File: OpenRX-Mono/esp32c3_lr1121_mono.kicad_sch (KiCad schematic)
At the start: 48 parts, among them T1 0900PC16J0042001E, U1 ESP32-C3FH4, U2 TLV75533PDQNR, U3 TS2306A 240GF MSM 9_C2976675, U4 LR1121IMLTRT, U5 OW7EL89CENUYO3YLC-32M, U7 RFX2401C, U8 SKY13414-485LF, X1 CJ17-400001010B20

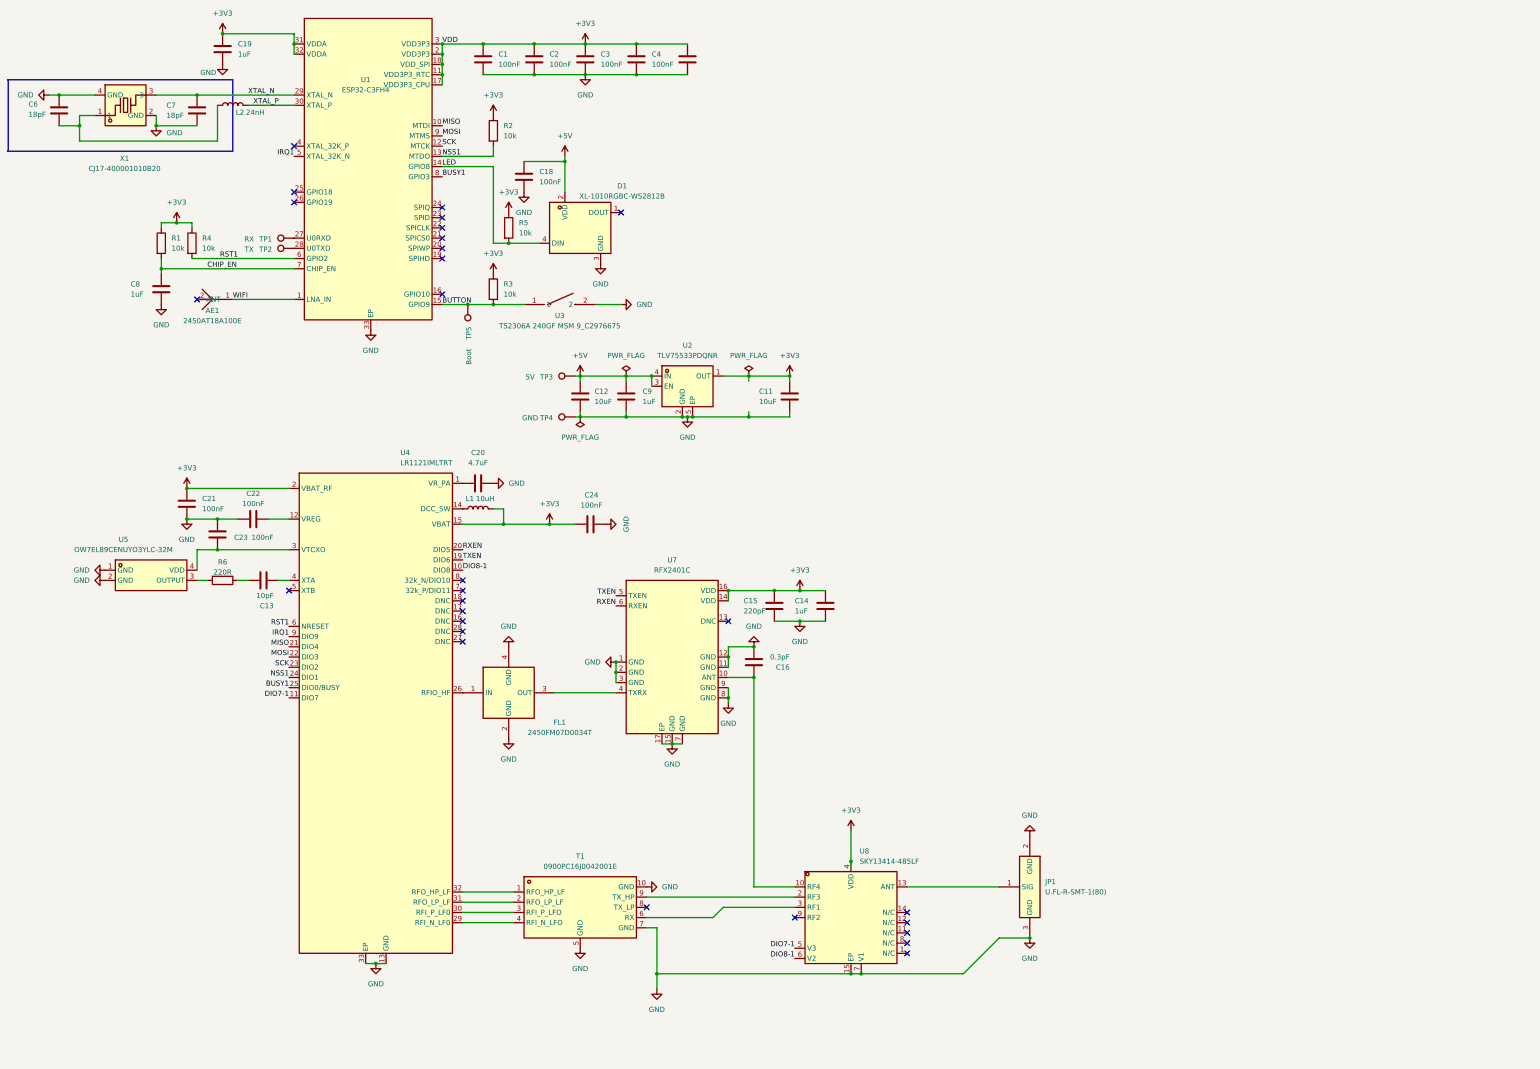
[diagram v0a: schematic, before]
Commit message: OpenRX Lite (UFL + molex)
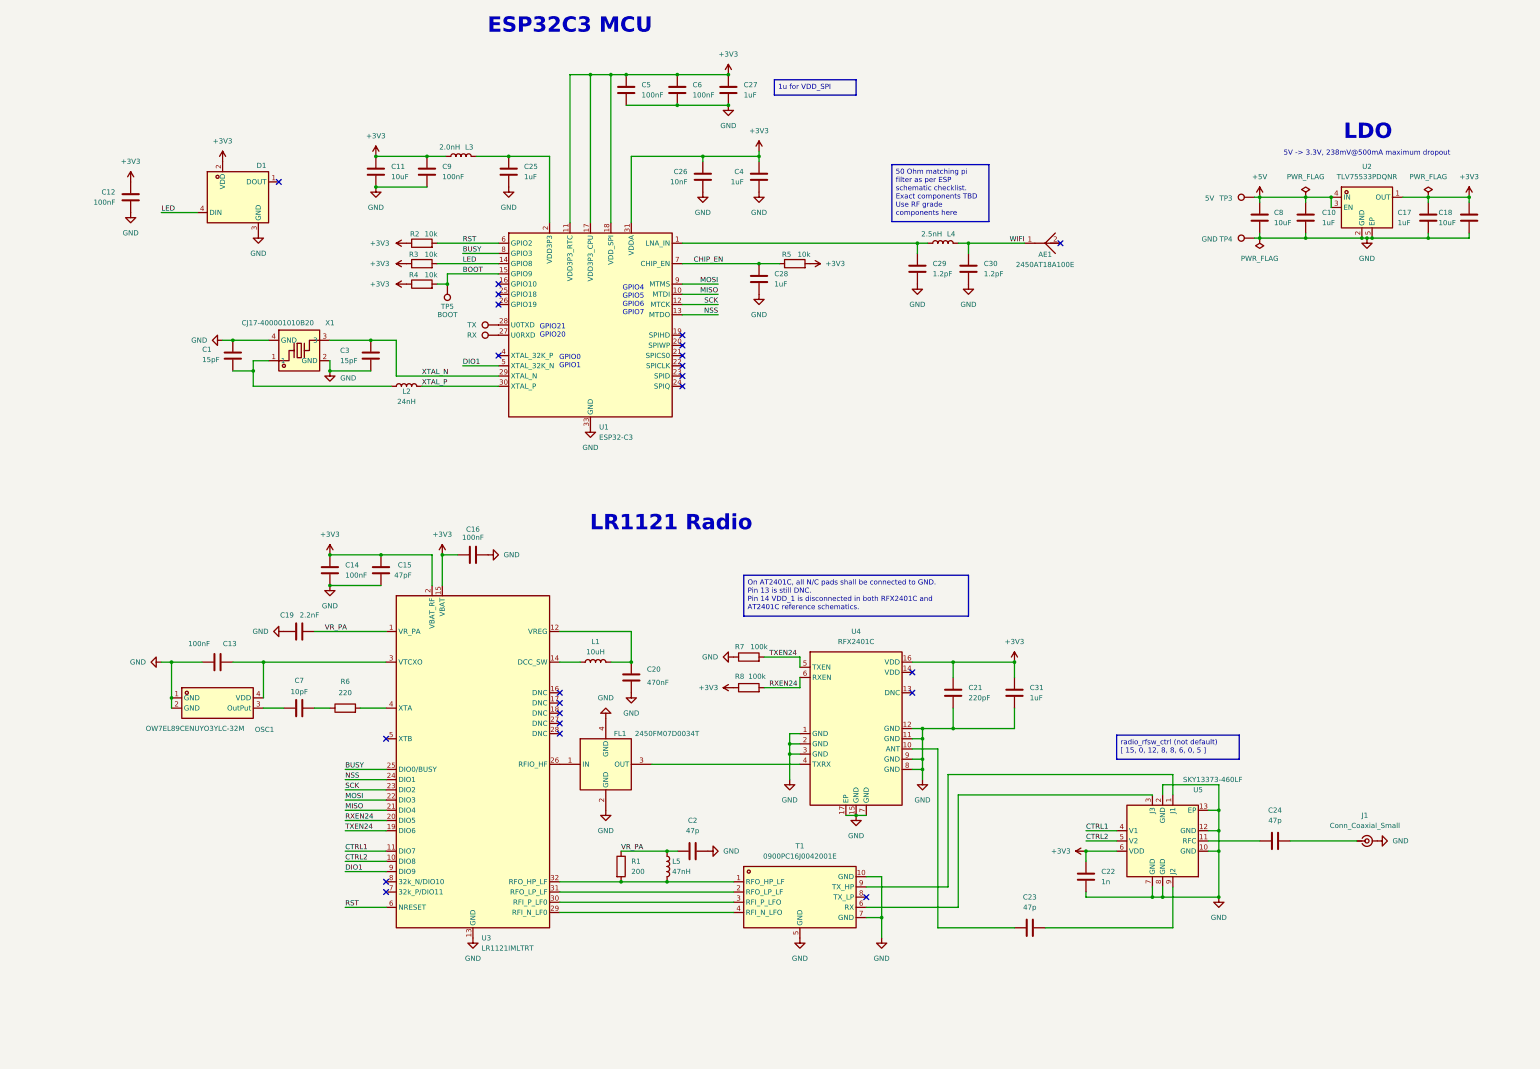
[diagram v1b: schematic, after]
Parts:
- removed JP1: U.FL-R-SMT-1(80), OpenRX-Shared:RF-SMD_FRF05002-JSS103M, symbol OpenRX-Shared:U.FL-R-SMT-1(80)
- removed U1: ESP32-C3FH4, OpenRX-Shared:QFN-32_L5.0-W5.0-P0.50-TL-EP3.7, symbol OpenRX-Shared:ESP32-C3FH4
- removed U3: TS2306A 240GF MSM 9_C2976675, OpenRX-Shared:SW-SMD_4P-L3.0-W2.0-P0.85-LS3.5, symbol OpenRX-Shared:TS2306A240GFMSM9_C2976675
- removed U4: LR1121IMLTRT, OpenRX-Shared:QFN-32_L5.0-W5.0-P0.50-BL-EP3.7, symbol OpenRX-Shared:LR1121IMLTRT
- removed U5: OW7EL89CENUYO3YLC-32M, OpenRX-Shared:OSC-SMD_4P-L2.0-W1.6-BL_TXC_7Z, symbol OpenRX-Shared:OW7EL89CENUYO3YLC-32M
- removed U7: RFX2401C, OpenRX-Shared:QFN-16_L3.0-W3.0-P0.50-BL-EP1.7, symbol OpenRX-Shared:RFX2401C
- removed U8: SKY13414-485LF, OpenRX-Shared:QFN-14_L2.0-W2.0-P0.45-BL-EP, symbol OpenRX-Shared:SKY13414-485LF
- added C10, C17, C25, C27, C28, C31: 1uF, Capacitor_SMD:C_0201_0603Metric, symbol Device:C
- added C26: 10nF, Capacitor_SMD:C_0201_0603Metric, symbol Device:C
- added C29, C30: 1.2pF, Capacitor_SMD:C_0201_0603Metric, symbol Device:C
- added J1: Conn_Coaxial_Small, Connector_Coaxial:U.FL_Hirose_U.FL-R-SMT-1_Vertical, symbol Connector:Conn_Coaxial_Small
- added L3: 2.0nH, Inductor_SMD:L_0201_0603Metric, symbol Device:L
- added L4: 2.5nH, Inductor_SMD:L_0201_0603Metric, symbol Device:L
- added L5: 47nH, Inductor_SMD:L_0402_1005Metric, symbol Device:L
- added OSC1: OW7EL89CENUYO3YLC-32M, OpenRX-Shared:OSC-SMD_4P-L2.0-W1.6-BL_TXC_7Z, symbol OpenRX-Shared:OW7EL89CENUYO3YLC-32M
- added R7, R8: 100k, Resistor_SMD:R_0201_0603Metric, symbol Device:R
- added U1: ESP32-C3, Package_DFN_QFN:QFN-32-1EP_5x5mm_P0.5mm_EP3.7x3.7mm, symbol MCU_Espressif:ESP32-C3
- added U3: LR1121IMLTRT, Package_DFN_QFN:QFN-32-1EP_5x5mm_P0.5mm_EP3.7x3.7mm, symbol OpenRX-Shared:LR1121IMLTRT
- added U4: RFX2401C, OpenRX-Shared:QFN-16_L3.0-W3.0-P0.50-BL-EP1.7, symbol OpenRX-Shared:RFX2401C
- added U5: SKY13373-460LF, OpenRX-Shared:QFN-12_EP_2x2_Pitch0.5mm, symbol OpenRX-Shared:SKY13373-460LF
- C1, C3: value 100nF -> 15pF; LCSC C76939 -> C85891; LCSC Part C76939 -> C85891
- C11: LCSC C15525 -> C76991; LCSC Part C15525 -> (none)
- C12: value 10uF -> 100nF; footprint Capacitor_SMD:C_0402_1005Metric -> Capacitor_SMD:C_0201_0603Metric; LCSC C15525 -> C76939; LCSC Part C15525 -> C76939
- C13: value 10pF -> 100nF; LCSC C76921 -> C76939; LCSC Part C76921 -> C76939
- C14, C9: value 1uF -> 100nF; LCSC C76935 -> C76939; LCSC Part C76935 -> C76939
- C15: value 220pF -> 47pF; LCSC C62548 -> C85908; LCSC Part C62548 -> C85908
- C16: value 0.3pF -> 100nF; LCSC C76927 -> C76939; LCSC Part C76927 -> C76939
- C18: value 100nF -> 10uF; footprint Capacitor_SMD:C_0201_0603Metric -> Capacitor_SMD:C_0402_1005Metric; LCSC C76939 -> C15525; LCSC Part C76939 -> C15525
- C19: value 1uF -> 2.2nF; LCSC C76935 -> C161488; LCSC Part C76935 -> (none)
- C2, C23, C24: value 100nF -> 47p; LCSC C76939 -> C85908; LCSC Part C76939 -> (none)
- C20: value 4.7uF -> 470nF; footprint Capacitor_SMD:C_0402_1005Metric -> Capacitor_SMD:C_0201_0603Metric; LCSC C23733 -> C85926; LCSC Part C23733 -> C85926
- C21: value 100nF -> 220pF; LCSC C76939 -> C907939; LCSC Part C76939 -> (none)
- C22: value 100nF -> 1n; LCSC C76939 -> C85934; LCSC Part C76939 -> (none)
- C4: value 100nF -> 1uF; LCSC C76939 -> C76935; LCSC Part C76939 -> C76935
- C6: value 18pF -> 100nF; LCSC C62164 -> C76939; LCSC Part C62164 -> C76939
- C7: value 18pF -> 10pF; LCSC C62164 -> C384956; LCSC Part C62164 -> C384956
- C8: value 1uF -> 10uF; footprint Capacitor_SMD:C_0201_0603Metric -> Capacitor_SMD:C_0402_1005Metric; LCSC C76935 -> C15525; LCSC Part C76935 -> C15525
- D1: LCSC C5349953 -> (none)
- L1: LCSC C1035 -> C194437; LCSC Part C1035 -> (none)
- R1: value 10k -> 200; LCSC C106225 -> C274337; LCSC Part C106225 -> (none)
- R6: value 220R -> 220; LCSC C274342 -> C2074788; LCSC Part C274342 -> C2074788
- T1: LCSC C19842466 -> (none)
- TP5: value Boot -> BOOT
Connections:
- net RST1 is gone; now on net BOOT: R4.2
- net +3V3: now also C12.1, C16.1, C18.1, C22.1, C6.1, C9.1, D1.2 (VDD), R5.2, C17.1, C26.1, C27.1, C31.1, L3.2, R8.1, U1.11 (VDD3P3_RTC), U1.17 (VDD3P3_CPU), U1.18 (VDD_SPI), U1.31 (VDDA), U1.32 (VDDA), U3.15 (VBAT), U3.2 (VBAT_RF), U4.16 (VDD), U5.6 (VDD); no longer C1.1, C19.1, C2.1, C24.2, C3.1, L1.2, R1.1, R5.1
- net +5V: now also C8.1, C10.1; no longer C12.1, C18.1, C9.1, D1.2 (VDD)
- net CHIP_EN: now also R5.1, C28.1, U1.7 (CHIP_EN); no longer C8.1, R1.2
- net LED: now also R3.2, U1.14 (GPIO8); no longer R5.2
- net MISO: now also U1.10 (MTDI), U3.21 (DIO4)
- net MOSI: now also U1.9 (MTMS), U3.22 (DIO3)
- net SCK: now also U1.12 (MTCK), U3.23 (DIO2)
- net WIFI: now also C30.1, L4.1
- net XTAL_N: now also C3.1, U1.29 (XTAL_N); no longer C7.1
- net XTAL_P: now also U1.30 (XTAL_P)
- net at TP1.1: now also U1.27 (U0RXD)
- net at TP2.1: now also U1.28 (U0TXD)
- net at L2.1, X1.1: now also C1.1; no longer C6.1
- net EP: now reaches C22.2
- net EP: now also C1.2, C11.2, C12.2, C13.1, C14.2, C15.2, C16.2, C18.2, C19.2, C2.2, C20.1, C21.2, C3.2, C4.2, C5.2, C6.2, C8.2, C9.2, D1.3 (GND), FL1.2 (GND), FL1.4 (GND), T1.10 (GND), T1.5 (GND), T1.7 (GND), TP4.1, U2.2 (GND), U2.5 (EP), X1.2 (GND), X1.4 (GND), C10.2, C17.2, C25.2, C26.2, C27.2, C28.2, C29.2, C30.2, C31.2, J1.2 (Ext), OSC1.1 (GND), OSC1.2 (GND), R7.1, U1.33 (GND), U3.13 (GND), U3.33 (EP), U4.1 (GND), U4.11 (GND), U4.12 (GND), U4.15 (GND), U4.17 (EP), U4.2 (GND), U4.3 (GND), U4.7 (GND), U4.8 (GND), U4.9 (GND), U5.10 (GND), U5.12 (GND), U5.13 (EP), U5.2 (GND), U5.7 (GND), U5.8 (GND)
- net at C23.2: now also U5.9 (J2)
- net at L1.1: now also U3.14 (DCC_SW)
- net at FL1.1 (IN): now also U3.26 (RFIO_HF)
- net at T1.4 (RFI_N_LFO): now also U3.29 (RFI_N_LF0)
- net at T1.3 (RFI_P_LFO): now also U3.30 (RFI_P_LF0)
- net at T1.2 (RFO_LP_LF): now also U3.31 (RFO_LP_LF)
- net at T1.1 (RFO_HP_LF): now also R1.2, L5.2, U3.32 (RFO_HP_LF)
- net at C13.2: now also OSC1.4 (VDD), U3.3 (VTCXO)
- net at T1.9 (TX_HP): now also U5.1 (J1)
- net at T1.6 (RX): now also U5.3 (J3)
- net at R6.1: now also C7.1; no longer C13.1
- net at FL1.3 (OUT): now also U4.4 (TXRX)
- net at R6.2: now also U3.4 (XTA)
- net BUTTON renamed BOOT
- net BOOT: now also U1.15 (GPIO9); no longer R3.2
- removed net GND: C1.2, C11.2, C12.2, C14.2, C15.2, C16.2, C18.2, C19.2, C2.2, C20.2, C21.2, C22.1, C23.1, C24.1, C3.2, C4.2, C5.2, C6.2, C7.2, C8.2, C9.2, D1.3 (GND), FL1.2 (GND), FL1.4 (GND), T1.10 (GND), T1.5 (GND), T1.7 (GND), TP4.1, U2.2 (GND), U2.5 (EP), X1.2 (GND), X1.4 (GND)
- net NSS1 renamed RST
- net RST: now also U1.6 (GPIO2), U3.6 (NRESET)
- new net: C25.1, L3.1, U1.2 (VDD3P3), U1.3 (VDD3P3)
- new net: C20.2, L1.2, U3.12 (VREG)
- new net: C7.2, OSC1.3 (OutPut)
- new net: C24.1, U5.11 (RFC)
- new net: C24.2, J1.1 (In)
- new net: C29.1, L4.2, U1.1 (LNA_IN)
- new net: C23.1, U4.10 (ANT)
- new net BUSY: U1.8 (GPIO3), U3.25 (DIO0/BUSY)
- new net CTRL1: U3.11 (DIO7), U5.4 (V1)
- new net CTRL2: U3.10 (DIO8), U5.5 (V2)
- new net DIO1: U1.5 (XTAL_32K_N), U3.9 (DIO9)
- new net NSS: U1.13 (MTDO), U3.24 (DIO1)
- new net RXEN24: R8.2, U3.20 (DIO5), U4.6 (RXEN)
- new net TXEN24: R7.2, U3.19 (DIO6), U4.5 (TXEN)
- new net VR_PA: C19.1, C2.1, L5.1, R1.1, U3.1 (VR_PA)
- no-connect marks 28 -> 23
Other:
- note added: "5V -> 3.3V, 238mV@500mA maximum dropout"
- note added: "ESP32C3 MCU"
- note added: "GPIO0 GPIO1"
- note added: "GPIO21 GPIO20"
- note added: "GPIO4 GPIO5 GPIO6 GPIO7"
- note added: "LDO"
- note added: "LR1121 Radio"

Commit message: annotate
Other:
- note added: "07/06/2026"
- note added: "1"
- note added: "Mono ELRS (2.4+900)"
- moved on the sheet: C10, C17, C18, C8, TP3, TP4, U2
